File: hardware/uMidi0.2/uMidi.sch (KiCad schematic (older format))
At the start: 20 parts, among them CON1 USB-MINI-B, IC1 ATXMEGA128A4U-M, P1 PDI, U1 74LS14

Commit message: Add mcu power distribution network
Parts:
- added C1, C2, C3, C4: 100n, symbol C
- added C5, C6: 10u, symbol C
- added L1: Bead, symbol INDUCTOR
- added L2: 10u, symbol INDUCTOR
- gave numbers to parts that had none: 15
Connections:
- wire segments 98 -> 101
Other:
- moved on the sheet: R1

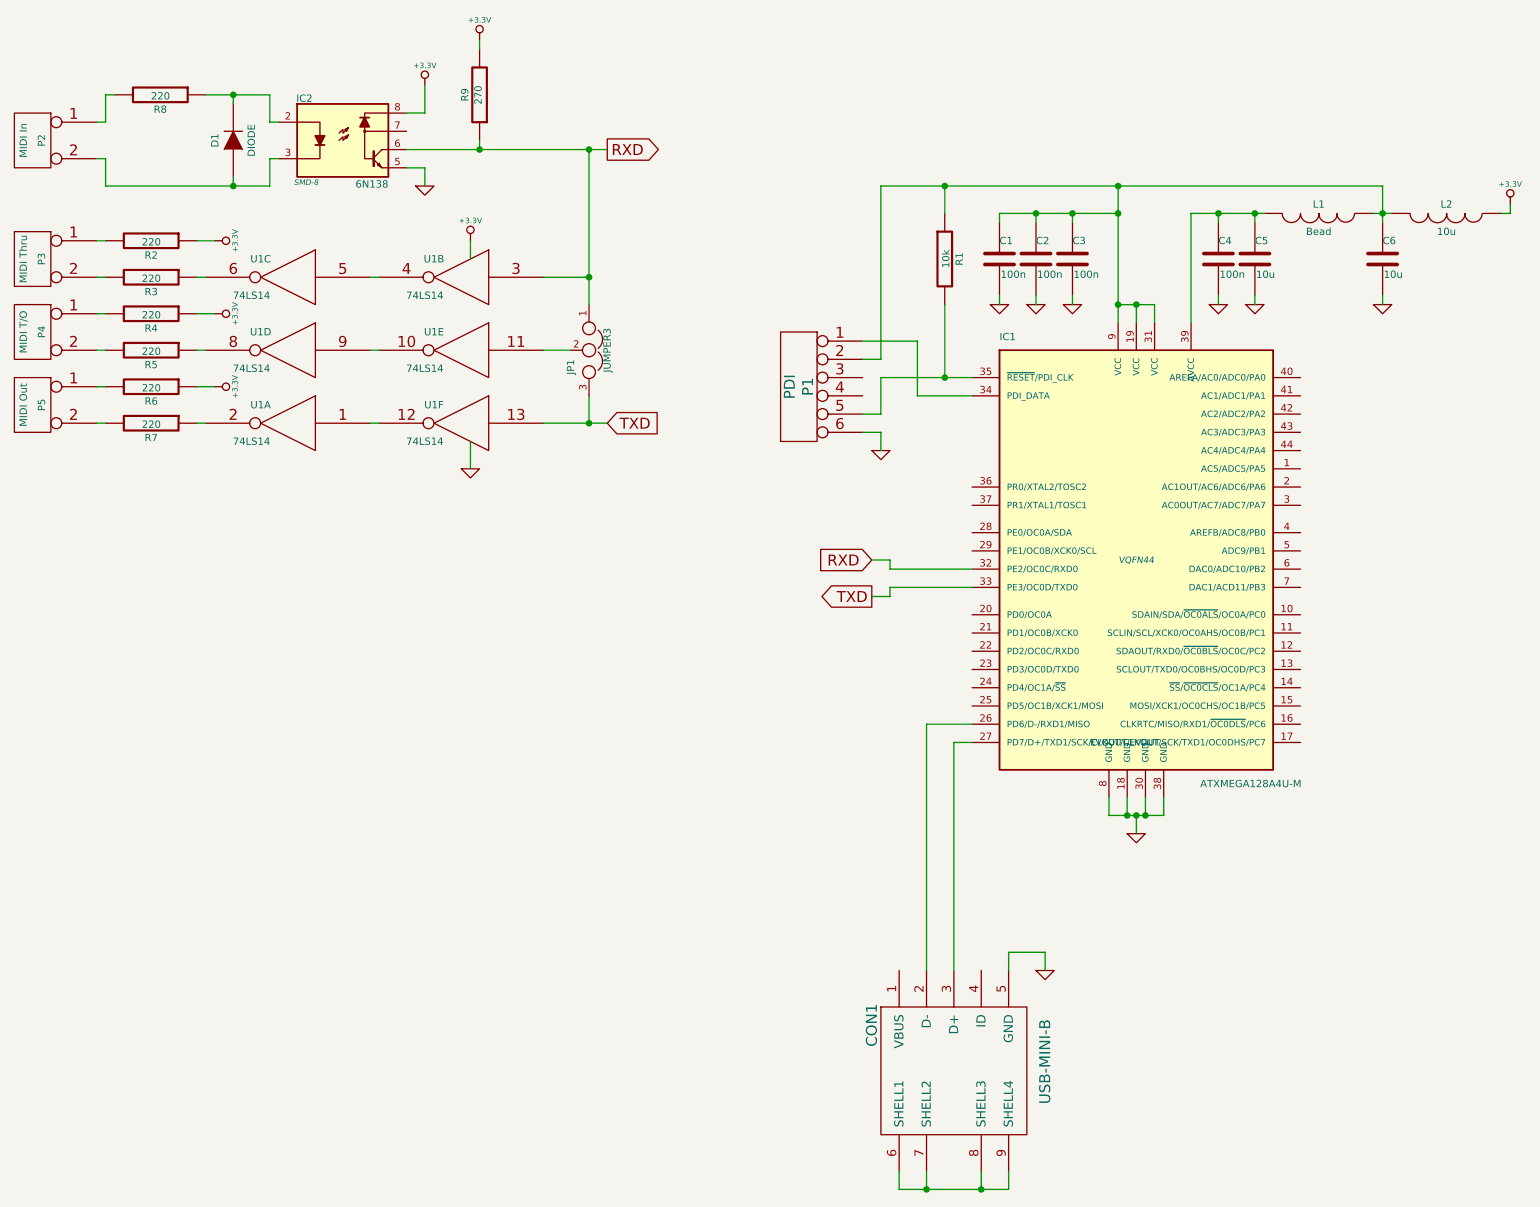
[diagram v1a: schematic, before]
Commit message: Add voltage regulator to schematic
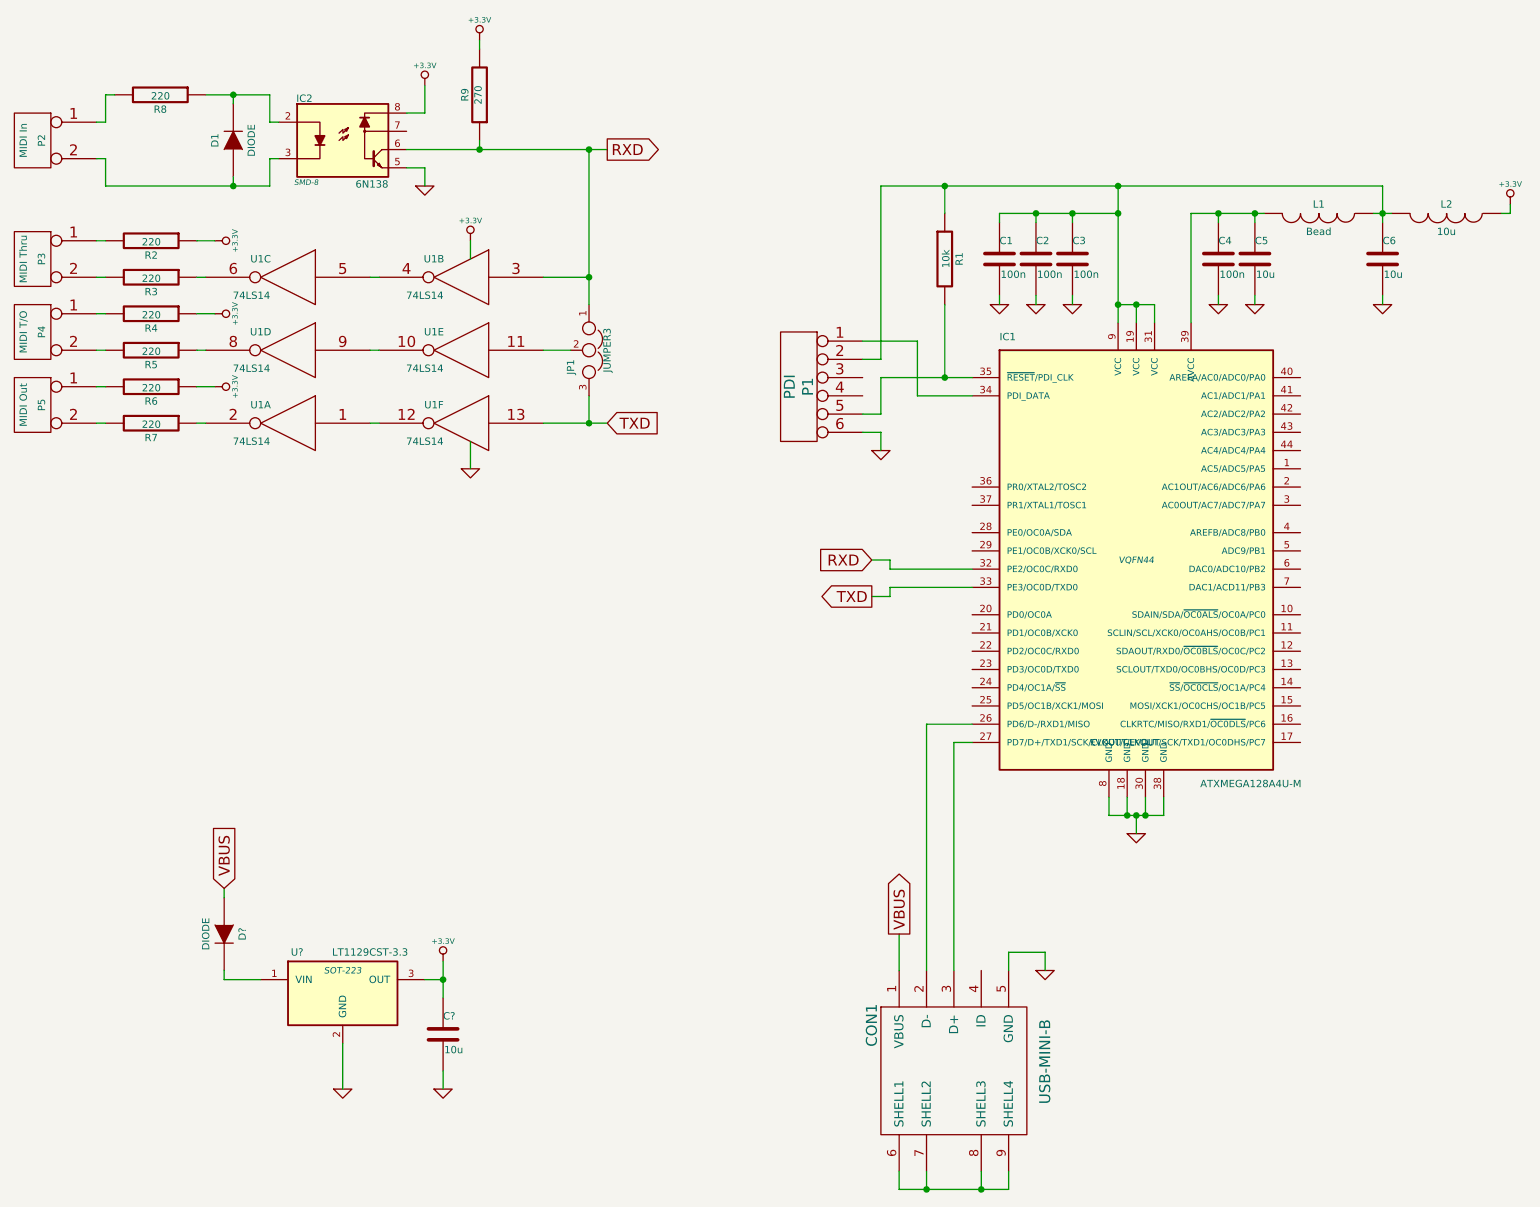
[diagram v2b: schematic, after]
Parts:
- added C?: 10u, symbol C
- added D?: DIODE, symbol DIODE
- added U?: LT1129CST-3.3, SOT-223, symbol LT1129CST-3.3
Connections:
- net +3.3V: now also C?.1, U?.3 (OUT)
- net GND: now also C?.2, U?.2 (GND)
- net VBUS: now reaches CON1.1 (VBUS)
- net VBUS: now also D?.1 (A)
- new net: D?.2 (K), U?.1 (VIN)
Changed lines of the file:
@@
 	7200 5150 7200 5250
 Wire Wire Line
-	7050 5150 7350 5150
+	7050 5150 7150 5150
+Wire Wire Line
+	7150 5150 7200 5150
+Wire Wire Line
+	7200 5150 7250 5150
+Wire Wire Line
+	7250 5150 7350 5150
 Wire Wire Line
 	7350 5150 7350 5050
@@
 	7200 2350 7200 2450
 Wire Wire Line
-	7100 2350 7300 2350
+	7100 2350 7200 2350
+Wire Wire Line
+	7200 2350 7300 2350
 Connection ~ 7200 2350
 Wire Wire Line
 	7300 2350 7300 2450
 Wire Wire Line
-	5800 2750 6300 2750
+	5800 2750 6150 2750
+Wire Wire Line
+	6150 2750 6300 2750
 Wire Wire Line
 	6150 2350 6150 2750
@@
 	3550 2100 3550 2000
 Wire Wire Line
-	3950 3000 4300 3000
+	3950 3000 4200 3000
+Wire Wire Line
+	4200 3000 4300 3000
 Wire Wire Line
 	6300 4750 6200 4750
@@
 	5900 7100 5900 7200
 Wire Wire Line
-	5900 7200 6500 7200
+	5900 7200 6050 7200
+Wire Wire Line
+	6050 7200 6350 7200
+Wire Wire Line
+	6350 7200 6500 7200
 Wire Wire Line
 	6500 7200 6500 7100
@@
 Connection ~ 4200 3000
 Wire Wire Line
-	4200 1500 4200 2350
+	4200 1500 4200 2200
+Wire Wire Line
+	4200 2200 4200 2350
 Wire Wire Line
 	4200 2200 3950 2200
@@
 $EndComp
 Wire Wire Line
-	1550 1700 2450 1700
+	1550 1700 2250 1700
+Wire Wire Line
+	2250 1700 2450 1700
 Wire Wire Line
 	2450 1700 2450 1550
@@
 Connection ~ 2250 1700
 Wire Wire Line
-	2100 1200 2450 1200
+	2100 1200 2250 1200
+Wire Wire Line
+	2250 1200 2450 1200
 Wire Wire Line
 	2450 1200 2450 1350
@@
 $EndComp
 Wire Wire Line
-	3200 1500 4300 1500
+	3200 1500 3600 1500
+Wire Wire Line
+	3600 1500 4200 1500
+Wire Wire Line
+	4200 1500 4300 1500
 Wire Wire Line
 	3600 1500 3600 1450
@@
 	7500 1850 7500 2450
 Wire Wire Line
-	7500 1850 7900 1850
+	7500 1850 7650 1850
+Wire Wire Line
+	7650 1850 7850 1850
+Wire Wire Line
+	7850 1850 7900 1850
 Wire Wire Line
 	7850 1900 7850 1850
@@
 $EndComp
 Wire Wire Line
-	6450 1850 7100 1850
-Wire Wire Line
-	7100 1700 7100 2450
+	6450 1850 6650 1850
+Wire Wire Line
+	6650 1850 6850 1850
+Wire Wire Line
+	6850 1850 7100 1850
+Wire Wire Line
+	7100 1700 7100 1850
+Wire Wire Line
+	7100 1850 7100 2350
+Wire Wire Line
+	7100 2350 7100 2450
 Wire Wire Line
 	6850 2350 6850 2300
@@
 	9250 1850 9250 1800
 Wire Wire Line
-	8500 1850 8600 1850
-Wire Wire Line
-	8550 1700 8550 1900
+	8500 1850 8550 1850
+Wire Wire Line
+	8550 1850 8600 1850
+Wire Wire Line
+	8550 1700 8550 1850
+Wire Wire Line
+	8550 1850 8550 1900
 Connection ~ 8550 1850
 Wire Wire Line
-	5800 1700 8550 1700
+	5800 1700 6150 1700
+Wire Wire Line
+	6150 1700 7100 1700
+Wire Wire Line
+	7100 1700 8550 1700
 Wire Wire Line
 	6150 1700 6150 1850
@@
 Connection ~ 6150 1700
 Connection ~ 7100 1700
+Wire Wire Line
+	5900 5800 5900 6000
+$Comp
+L LT1129CST-3.3 U?
+U 1 1 53CAB726
+P 2850 6100
+F 0 "U?" H 2600 6300 40  0000 C CNN
+F 1 "LT1129CST-3.3" H 3000 6300 40  0000 C CNN
+F 2 "SOT-223" H 2850 6200 35  0000 C CIN
+F 3 "" H 2850 6100 60  0000 C CNN
+	1    2850 6100
+	1    0    0    -1
+$EndComp
+Text GLabel 5900 5800 1    60   Output ~ 0
+VBUS
+Text GLabel 2200 5550 1    60   Input ~ 0
+VBUS
+$Comp
+L DIODE D?
+U 1 1 53CAB822
+P 2200 5800
+F 0 "D?" H 2200 5900 40  0000 C CNN
+F 1 "DIODE" H 2200 5700 40  0000 C CNN
+F 2 "" H 2200 5800 60  0000 C CNN
+F 3 "" H 2200 5800 60  0000 C CNN
+	1    2200 5800
+	0    1    1    0
+$EndComp
+Wire Wire Line
+	2200 5600 2200 5550
+Wire Wire Line
+	2200 6000 2200 6050
+Wire Wire Line
+	2200 6050 2400 6050
+$Comp
+L GND #PWR?
+U 1 1 53CAB9F8
+P 2850 6650
+F 0 "#PWR?" H 2850 6650 30  0001 C CNN
+F 1 "GND" H 2850 6580 30  0001 C CNN
+F 2 "" H 2850 6650 60  0000 C CNN
+F 3 "" H 2850 6650 60  0000 C CNN
+	1    2850 6650
+	1    0    0    -1
+$EndComp
+Wire Wire Line
+	2850 6650 2850 6400
+$Comp
+L C C?
+U 1 1 53CABAC9
+P 3400 6350
+F 0 "C?" H 3400 6450 40  0000 L CNN
+F 1 "10u" H 3406 6265 40  0000 L CNN
+F 2 "" H 3438 6200 30  0000 C CNN
+F 3 "" H 3400 6350 60  0000 C CNN
+	1    3400 6350
+	1    0    0    -1
+$EndComp
+$Comp
+L GND #PWR?
+U 1 1 53CABAD4
+P 3400 6650
+F 0 "#PWR?" H 3400 6650 30  0001 C CNN
+F 1 "GND" H 3400 6580 30  0001 C CNN
+F 2 "" H 3400 6650 60  0000 C CNN
+F 3 "" H 3400 6650 60  0000 C CNN
+	1    3400 6650
+	1    0    0    -1
+$EndComp
+Wire Wire Line
+	3400 6650 3400 6550
+Wire Wire Line
+	3400 5950 3400 6050
+Wire Wire Line
+	3400 6050 3400 6150
+Wire Wire Line
+	3400 6050 3300 6050
+$Comp
+L +3.3V #PWR?
+U 1 1 53CABBFC
+P 3400 5950
+F 0 "#PWR?" H 3400 5910 30  0001 C CNN
+F 1 "+3.3V" H 3400 6060 30  0000 C CNN
+F 2 "" H 3400 5950 60  0000 C CNN
+F 3 "" H 3400 5950 60  0000 C CNN
+	1    3400 5950
+	1    0    0    -1
+$EndComp
+Connection ~ 3400 6050
 $EndSCHEMATC
